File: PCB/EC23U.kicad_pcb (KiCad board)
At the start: 2 copper layers, 77.1 x 137.6 mm, 84 parts, among them J1 JST, J2 RGB, SW1 BOOT0, SW10 EC_SW, SW11 EC_SW, SW12 EC_SW, SW13 EC_SW, SW14 EC_SW, SW15 EC_SW, SW16 EC_SW, SW17 EC_SW, SW18 EC_SW, SW19 EC_SW, SW2 EC_SW, SW20 EC_SW, SW21 EC_SW, SW22 EC_SW, SW23 EC_SW, SW24 EC_SW, SW25 EC_SW, SW26 EC_SW, SW27 EC_SW, SW28 EC_SW, SW3 EC_SW, SW4 EC_SW, SW5 EC_SW, SW6 EC_SW, SW7 EC_SW, SW8 EC_SW, SW9 EC_SW, U1 STM32F401CBUx, U2 XC6206PxxxMR, U3 74HC4051, U4 OPA350, U5 SN74AHCT1G125, Y1 8 MHz

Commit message: Kicad 7 update and change of resistor value
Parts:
- R15: value 100k -> 47k

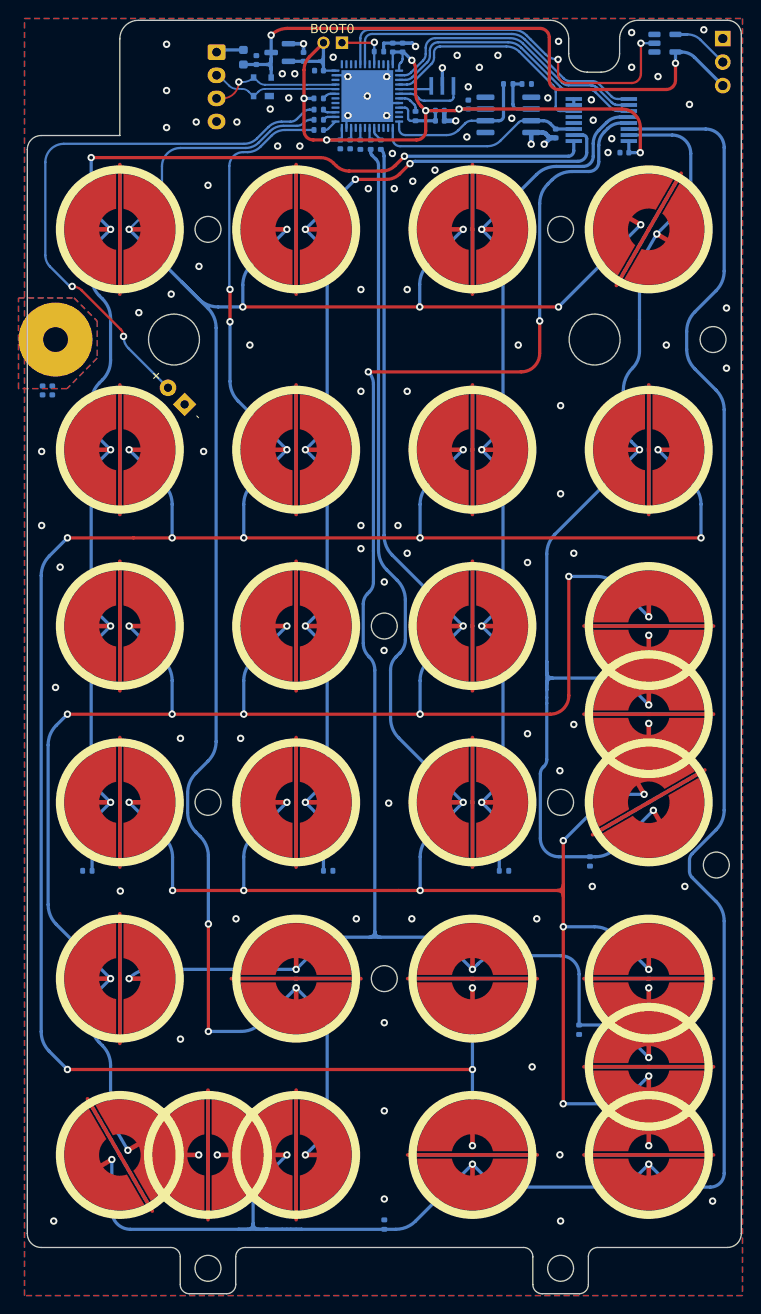
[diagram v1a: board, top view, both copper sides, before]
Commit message: Updated to `Rev 1.1`
Updated the title block in schematics to reflect company name and updated EC pads to latest model.
This update isn't critical, hence the lack of proper `Rev` update in README.
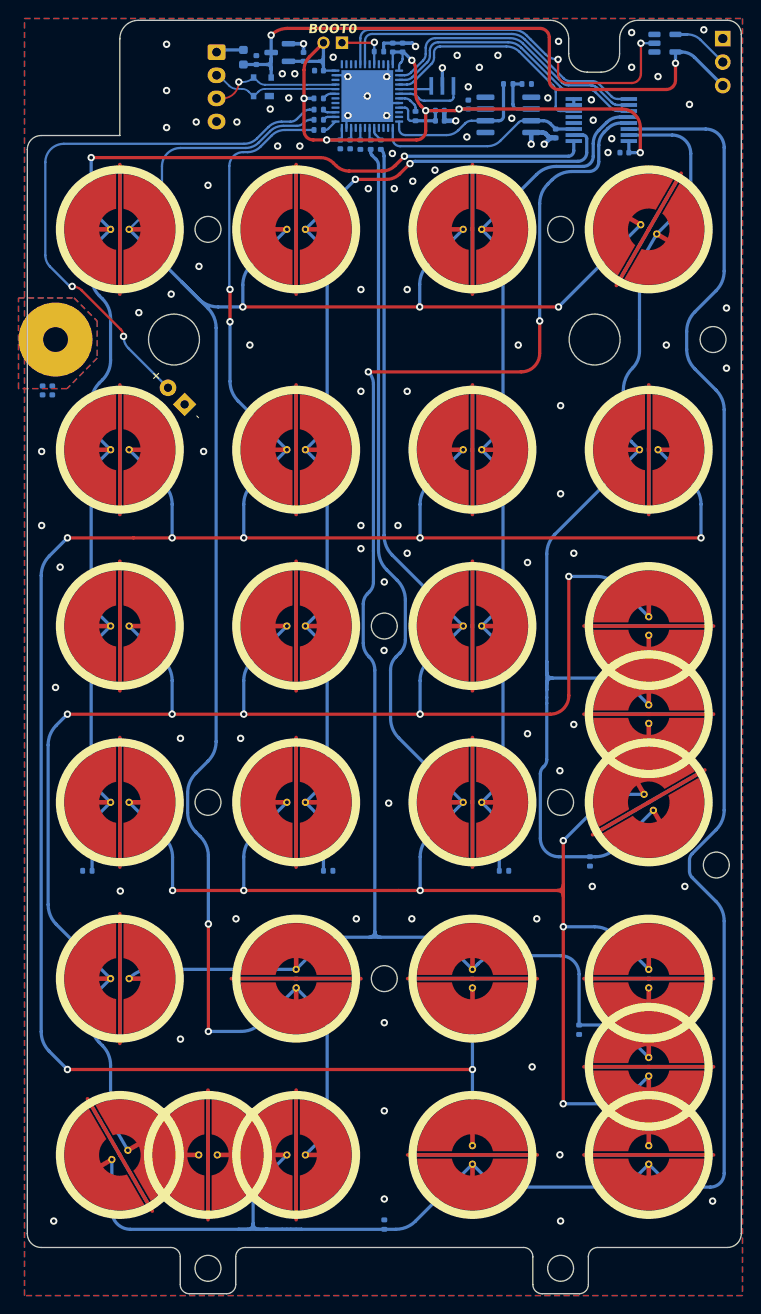
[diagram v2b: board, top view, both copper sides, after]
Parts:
- removed the G*** at (161.4, 157.0)
- removed the G*** at (126.8, 60.9)
- removed the G*** at (152.5, 82.6)
- added G***: LOGO, cipulot_parts:Cipulot_Logo_Silk, B.Cu at (152.7, 82.4)
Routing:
- net STROBE_3: vias 14 -> 6
- net STROBE_2: vias 12 -> 5
- net STROBE_1: vias 15 -> 9
- net STROBE_0: vias 11 -> 5
- net SENSE_5: vias 5 -> 0
- net SENSE_4: vias 7 -> 2
- net SENSE_3: vias 5 -> 0
- net SENSE_2: vias 4 -> 0
- net SENSE_1: vias 6 -> 2
- net SENSE_0: vias 6 -> 2
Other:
- board text added: "EC23U"
- board text added: "Rev 1.1"
